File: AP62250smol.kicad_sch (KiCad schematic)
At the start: 13 parts, among them J1 Heatsink Pads, J2 Connector Pads, U1 AP62250Z6

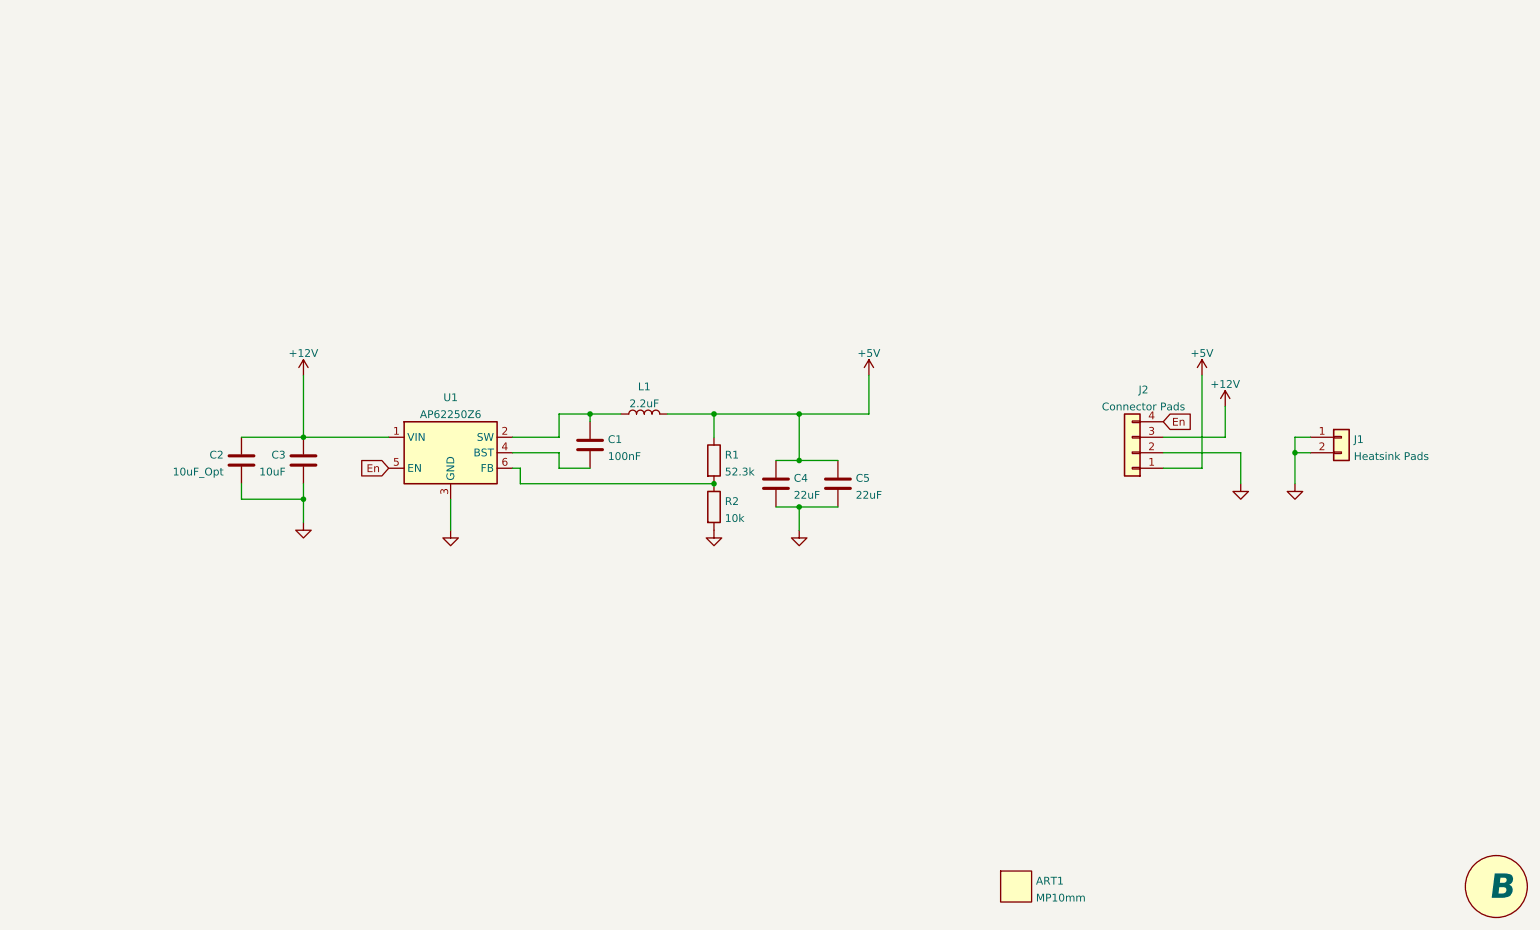
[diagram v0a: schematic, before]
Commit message: I am a liar who lies. This is RevB. Major revision changes board dimensions and increases input capacitor to 1206
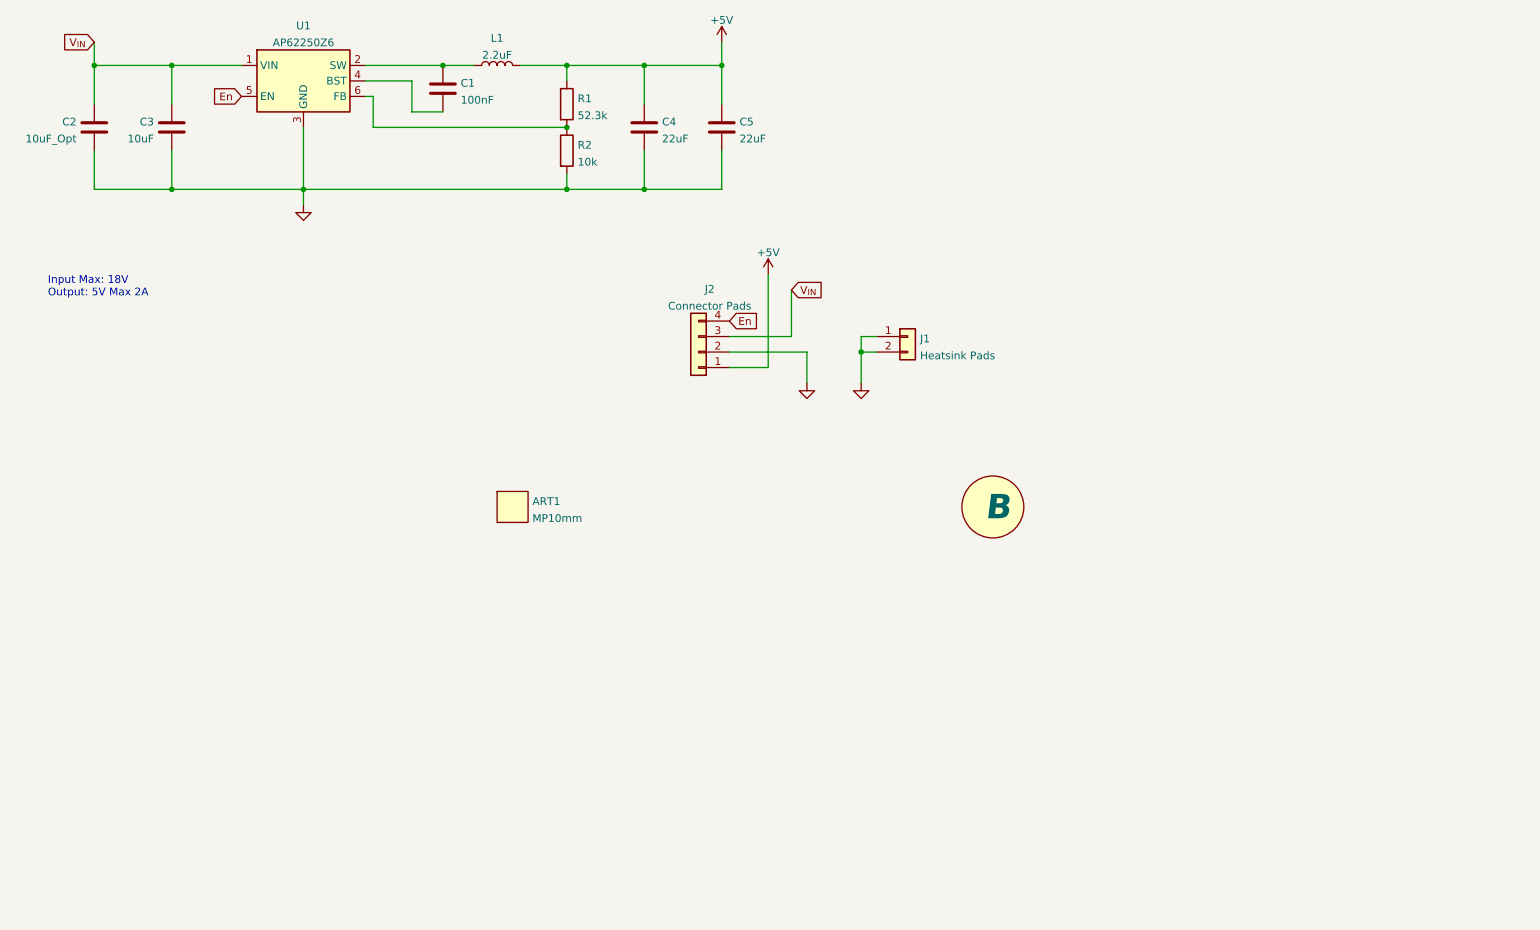
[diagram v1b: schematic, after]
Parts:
- C2, C3: footprint Capacitor_SMD:C_0805_2012Metric -> Capacitor_SMD:C_1206_3216Metric
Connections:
- net +12V renamed V_{IN}
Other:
- note added: "Input Max: 18V Output: 5V Max 2A"
- moved on the sheet: ART1, C1, C2, C3, C4, C5, J1, J2, L1, R1, R2, U1

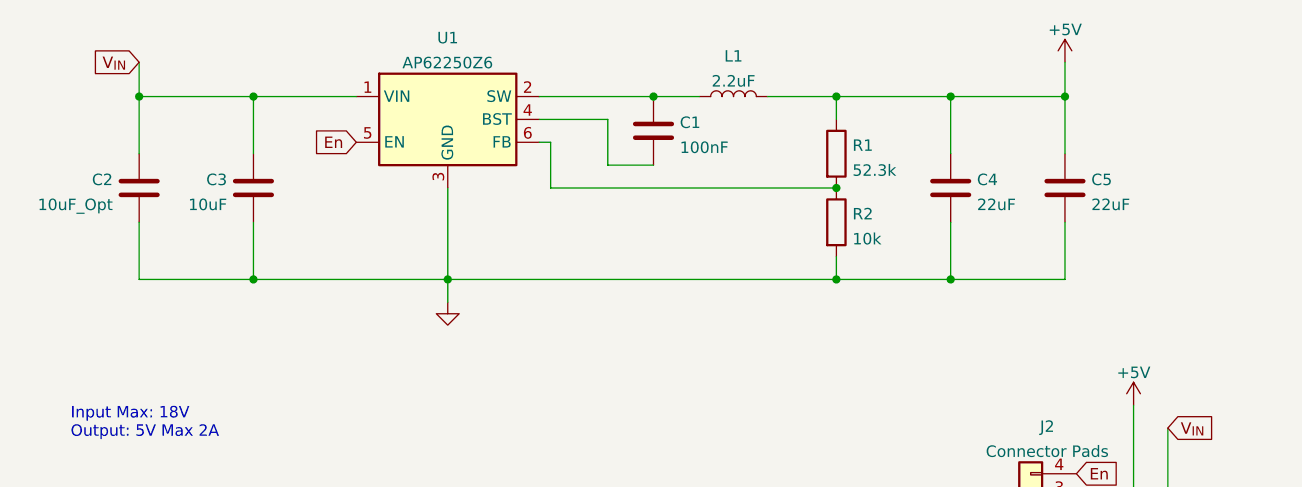
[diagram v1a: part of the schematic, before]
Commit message: Removed second input capacitor.
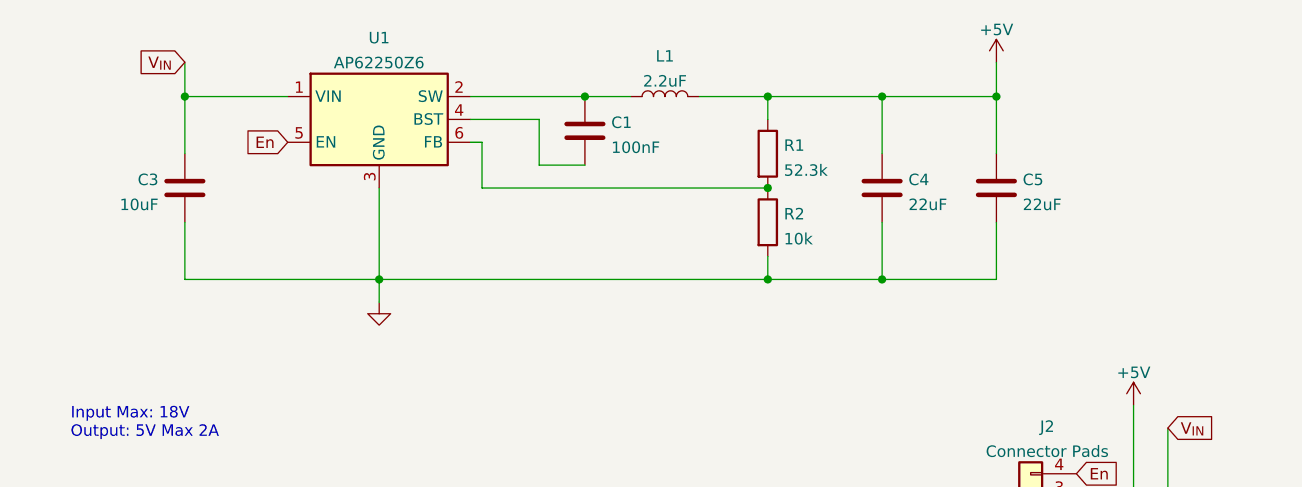
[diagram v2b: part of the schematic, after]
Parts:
- removed C2: 10uF_Opt, Capacitor_SMD:C_1206_3216Metric, symbol Device:C
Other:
- moved on the sheet: C1, C3, C4, C5, L1, R1, R2, U1

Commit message: Actually, RevC
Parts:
- MISC1: value B -> C
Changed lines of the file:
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@@
       (effects (font (size 1.27 1.27)) hide)
     )
-    (property "Value" "B" (id 1) (at 182.88 111.76 0)
+    (property "Value" "C" (id 1) (at 182.88 111.76 0)
       (effects (font (size 4 4) bold italic) (justify left))
     )
@@
     )
     (path "/b59ecb45-aa0d-46e4-bca5-813980b0b68f"
-      (reference "MISC1") (unit 1) (value "B") (footprint "MikeFootprintLib:RevisionSymbol_Small")
+      (reference "MISC1") (unit 1) (value "C") (footprint "MikeFootprintLib:RevisionSymbol_Small")
     )
     (path "/75694f88-736a-46d6-b554-515f720e0555"

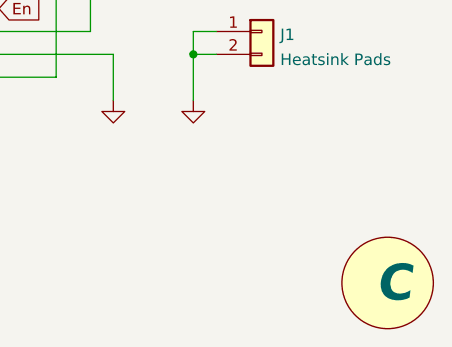
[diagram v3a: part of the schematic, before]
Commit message: Updated IC footprint to allow 0.2mm spacing between pads. This allows for solder mask between pads if ordering green solder mask from JLCPCB
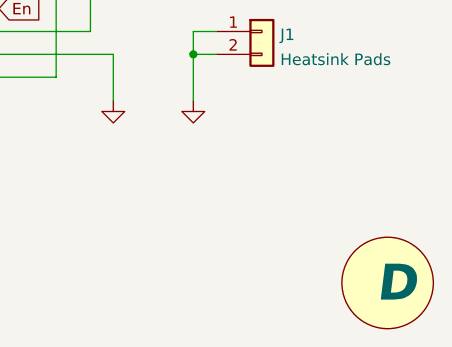
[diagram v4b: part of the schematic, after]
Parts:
- MISC1: value C -> D
- U1: footprint Package_TO_SOT_SMD:SOT-563 -> MikeFootprintLib:SOT-563_wider_clearance
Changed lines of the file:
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@@
     (property "Reference" "U1" (id 0) (at 63.5 32.8634 0))
     (property "Value" "AP62250Z6" (id 1) (at 63.5 35.6385 0))
-    (property "Footprint" "Package_TO_SOT_SMD:SOT-563" (id 2) (at 63.5 41.91 0)
+    (property "Footprint" "MikeFootprintLib:SOT-563_wider_clearance" (id 2) (at 63.5 41.91 0)
       (effects (font (size 1.27 1.27)) hide)
     )
@@
       (effects (font (size 1.27 1.27)) hide)
     )
-    (property "Value" "C" (id 1) (at 182.88 111.76 0)
+    (property "Value" "D" (id 1) (at 182.88 111.76 0)
       (effects (font (size 4 4) bold italic) (justify left))
     )
@@
     )
     (path "/b59ecb45-aa0d-46e4-bca5-813980b0b68f"
-      (reference "MISC1") (unit 1) (value "C") (footprint "MikeFootprintLib:RevisionSymbol_Small")
+      (reference "MISC1") (unit 1) (value "D") (footprint "MikeFootprintLib:RevisionSymbol_Small")
     )
     (path "/75694f88-736a-46d6-b554-515f720e0555"
@@
     )
     (path "/28d4f2e4-98ef-4d05-8fc8-12f2a6290689"
-      (reference "U1") (unit 1) (value "AP62250Z6") (footprint "Package_TO_SOT_SMD:SOT-563")
-    )
-  )
+      (reference "U1") (unit 1) (value "AP62250Z6") (footprint "MikeFootprintLib:SOT-563_wider_clearance")
+    )
+  )
